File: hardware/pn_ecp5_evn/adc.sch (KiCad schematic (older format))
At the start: 32 parts, among them U801 THS4551, U802 LT6657BHMS8-2.5

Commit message: first pass footprint assignment on pn r0
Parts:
- C801, C802, C805, C806, C807, C808, C810, C811, C813: footprint (none) -> Capacitor_SMD:C_0402_1005Metric
- C803, C804, C809, C812: footprint (none) -> Capacitor_SMD:C_0603_1608Metric
- R801, R802: value R_Small -> 10k; footprint (none) -> Resistor_SMD:R_0402_1005Metric
- R803, R804, R805, R806, R807, R808, R809, R810, R811, R812, R813, R814, R815, R816, R817: footprint (none) -> Resistor_SMD:R_0402_1005Metric
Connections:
- net +3V3: no longer R801.1
- net BUF_~PD: now also R801.1, R802.1, U802.3 (~SHDN); no longer R801.2
- net GND: now also R801.2
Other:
- moved on the sheet: C807, C808, C809, R801, R802, R807, U802

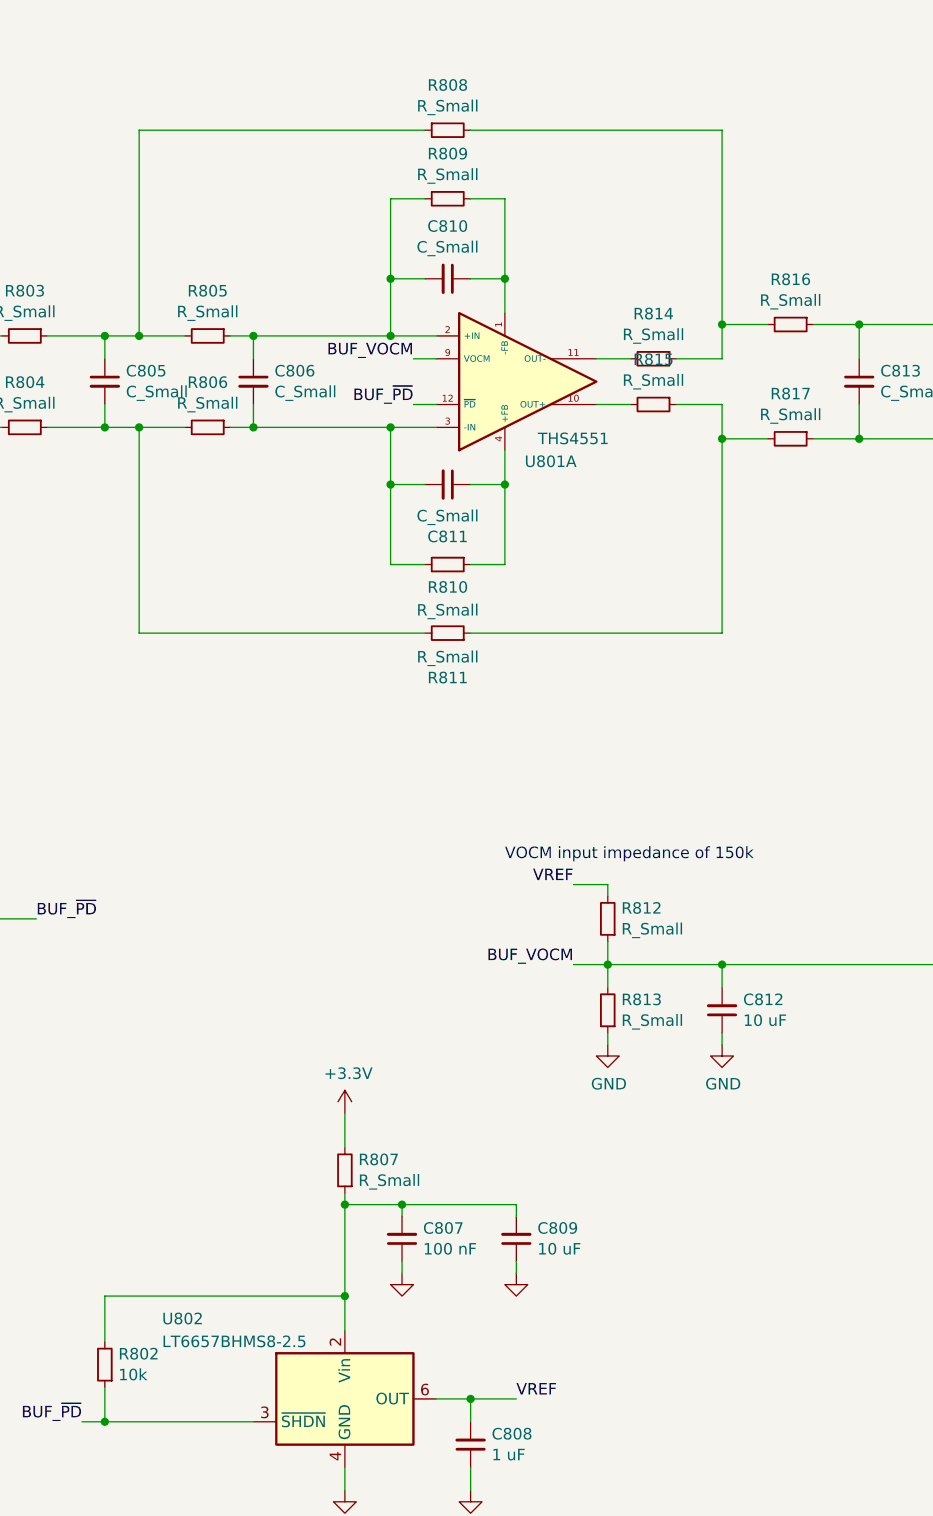
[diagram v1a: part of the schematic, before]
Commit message: started component placement on phase noise analyzer
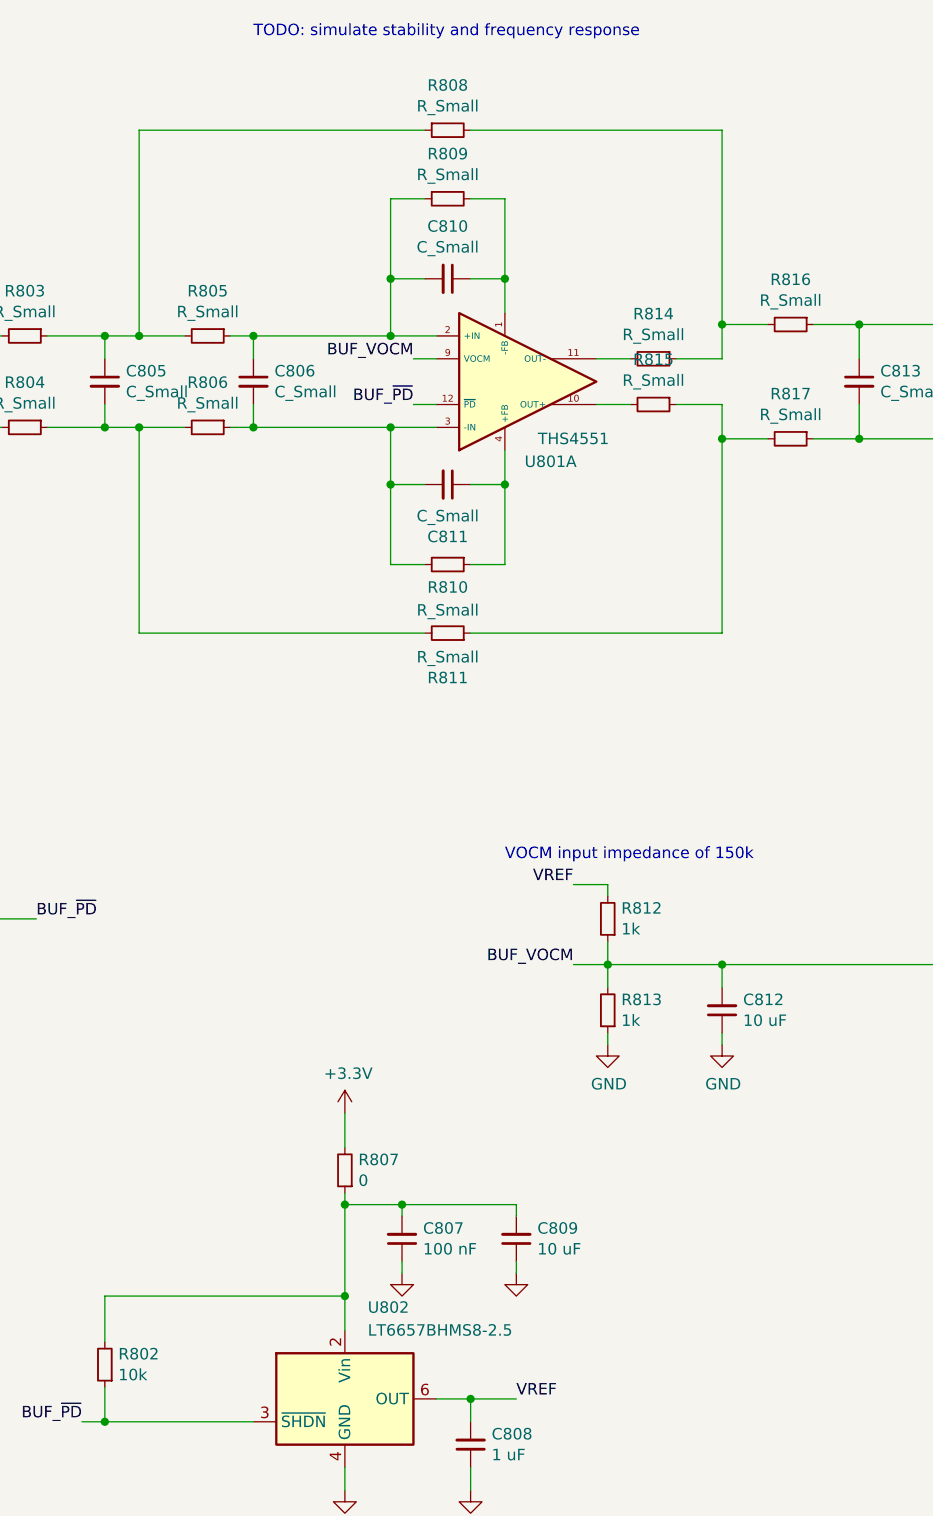
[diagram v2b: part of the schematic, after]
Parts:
- R807: value R_Small -> 0
- R812, R813: value R_Small -> 1k
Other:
- note added: "TODO: simulate stability and frequency response"
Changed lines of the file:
@@
 U 1 1 5FA4D542
 P 4700 6700
-F 0 "U802" H 3900 7050 50  0000 L CNN
-F 1 "LT6657BHMS8-2.5" H 3900 6950 50  0000 L CNN
+F 0 "U802" H 4800 7100 50  0000 L CNN
+F 1 "LT6657BHMS8-2.5" H 4800 7000 50  0000 L CNN
 F 2 "Package_SO:MSOP-8_3x3mm_P0.65mm" H 4800 7050 50  0001 L CIN
 F 3 "https://www.analog.com/media/en/technical-documentation/data-sheets/6657fd.pdf" H 4750 6350 50  0001 C CIN
@@
 P 5850 4600
 F 0 "R812" H 5791 4554 50  0000 R CNN
-F 1 "R_Small" H 5791 4645 50  0000 R CNN
+F 1 "1k" H 5791 4645 50  0000 R CNN
 F 2 "Resistor_SMD:R_0402_1005Metric" H 5850 4600 50  0001 C CNN
 F 3 "~" H 5850 4600 50  0001 C CNN
@@
 P 5850 5000
 F 0 "R813" H 5791 4954 50  0000 R CNN
-F 1 "R_Small" H 5791 5045 50  0000 R CNN
+F 1 "1k" H 5791 5045 50  0000 R CNN
 F 2 "Resistor_SMD:R_0402_1005Metric" H 5850 5000 50  0001 C CNN
 F 3 "~" H 5850 5000 50  0001 C CNN
@@
 P 4700 5700
 F 0 "R807" H 4641 5654 50  0000 R CNN
-F 1 "R_Small" H 4641 5745 50  0000 R CNN
+F 1 "0" H 4641 5745 50  0000 R CNN
 F 2 "Resistor_SMD:R_0402_1005Metric" H 4700 5700 50  0001 C CNN
 F 3 "~" H 4700 5700 50  0001 C CNN
@@
 	3550 6800 3650 6800
 Connection ~ 3650 6800
+Text Notes 4300 750  0    50   ~ 0
+TODO: simulate stability and frequency response
 $EndSCHEMATC

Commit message: work on routing phase noise downconverter
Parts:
- U801: footprint Package_CSP:LFCSP-24-1EP_4x4mm_P0.5mm_EP2.5x2.5mm -> Package_DFN_QFN:VQFN-16-1EP_3x3mm_P0.5mm_EP1.6x1.6mm
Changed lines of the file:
@@
 F 0 "U801" H 5600 2600 50  0000 C CNN
 F 1 "THS4551" H 5700 2500 50  0000 C CNN
-F 2 "Package_CSP:LFCSP-24-1EP_4x4mm_P0.5mm_EP2.5x2.5mm" H 5400 1850 50  0001 C CNN
+F 2 "Package_DFN_QFN:VQFN-16-1EP_3x3mm_P0.5mm_EP1.6x1.6mm" H 5400 1850 50  0001 C CNN
 F 3 "https://www.ti.com/lit/ds/symlink/ths4551.pdf" H 3700 3450 50  0001 C CNN
 	1    5400 2250
@@
 F 0 "U801" H 1830 6646 50  0000 L CNN
 F 1 "THS4551" H 1830 6555 50  0000 L CNN
-F 2 "Package_CSP:LFCSP-24-1EP_4x4mm_P0.5mm_EP2.5x2.5mm" H 1550 6200 50  0001 C CNN
+F 2 "Package_DFN_QFN:VQFN-16-1EP_3x3mm_P0.5mm_EP1.6x1.6mm" H 1550 6200 50  0001 C CNN
 F 3 "https://www.ti.com/lit/ds/symlink/ths4551.pdf" H -150 7800 50  0001 C CNN
 	2    1550 6600

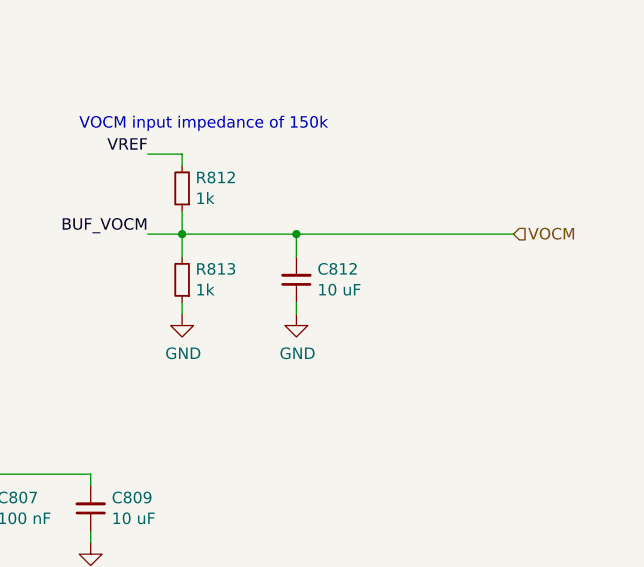
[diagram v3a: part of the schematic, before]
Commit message: layout of phase noise downconverter
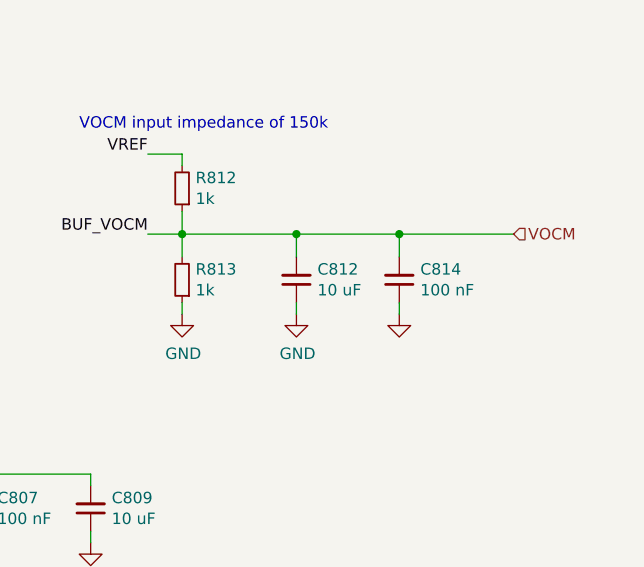
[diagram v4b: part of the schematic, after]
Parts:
- added C814: 100 nF, Capacitor_SMD:C_0402_1005Metric, symbol Device:C_Small
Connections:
- net GND: now also C814.1
- net VOCM: now also C814.2
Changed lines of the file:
@@
 	6950 2500 7400 2500
 Wire Wire Line
-	7300 4800 6350 4800
+	7300 4800 6800 4800
 Connection ~ 6350 4800
 Text HLabel 2850 4600 0    50   Input ~ 0
@@
 Text Notes 4300 750  0    50   ~ 0
 TODO: simulate stability and frequency response
+$Comp
+L Device:C_Small C814
+U 1 1 5F478B8F
+P 6800 5000
+F 0 "C814" H 6708 4954 50  0000 R CNN
+F 1 "100 nF" H 6708 5045 50  0000 R CNN
+F 2 "Capacitor_SMD:C_0402_1005Metric" H 6800 5000 50  0001 C CNN
+F 3 "~" H 6800 5000 50  0001 C CNN
+	1    6800 5000
+	-1   0    0    1
+$EndComp
+$Comp
+L power:GND #PWR0306
+U 1 1 5F478B95
+P 6800 5150
+F 0 "#PWR0306" H 6800 4900 50  0001 C CNN
+F 1 "GND" H 6805 4977 50  0001 C CNN
+F 2 "" H 6800 5150 50  0001 C CNN
+F 3 "" H 6800 5150 50  0001 C CNN
+	1    6800 5150
+	1    0    0    -1
+$EndComp
+Wire Wire Line
+	6800 5150 6800 5100
+Wire Wire Line
+	6800 4900 6800 4800
+Connection ~ 6800 4800
+Wire Wire Line
+	6800 4800 6350 4800
 $EndSCHEMATC
